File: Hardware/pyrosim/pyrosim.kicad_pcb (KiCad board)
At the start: 2 copper layers, 13 x 15.5 mm, 7 parts, among them J1 Conn_01x04_Pin

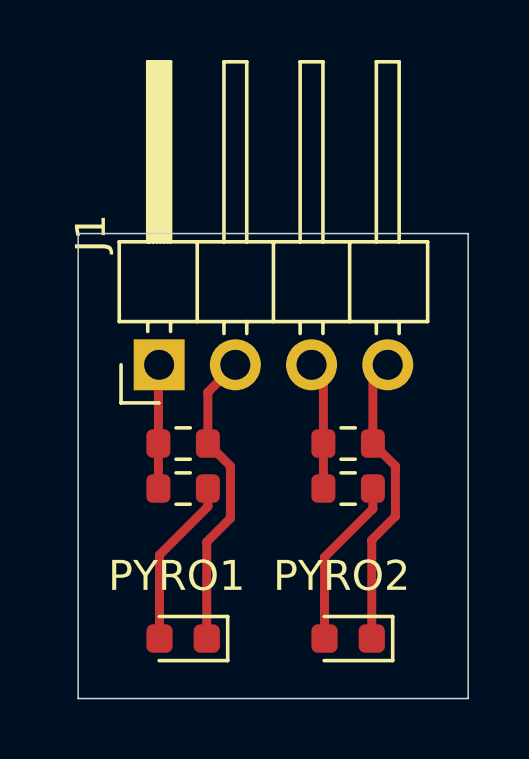
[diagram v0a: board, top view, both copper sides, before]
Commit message: APRS emulation testing, trying to get long packets working
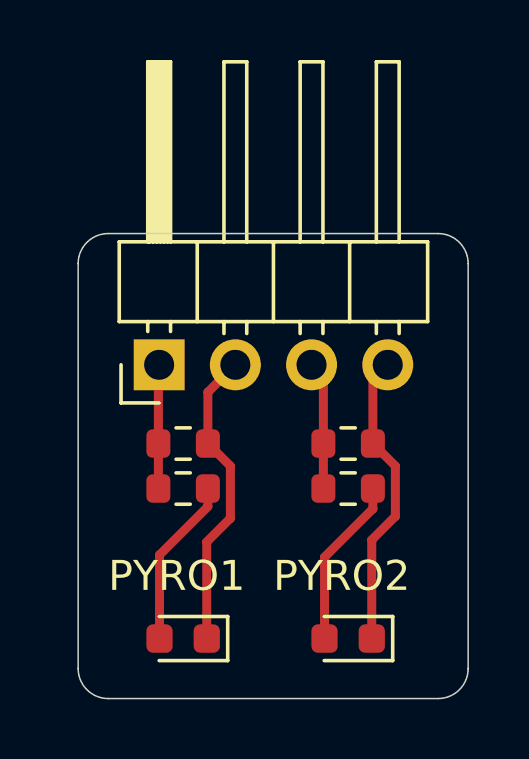
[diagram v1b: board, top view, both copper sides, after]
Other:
- outline, holes or cut-outs redrawn
- board text added: "PYROSIM"
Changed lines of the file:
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@@
 		)
 		(property "Value" "470R"
-			(at 0 1.43 360)
+			(at 0 1.43 0)
 			(layer "F.Fab")
 			(effects
@@
 		)
 		(fp_text user "${REFERENCE}"
-			(at 0 0 360)
+			(at 0 0 0)
 			(layer "F.Fab")
 			(effects
@@
 			(at 4.385 -2.27 90)
 			(layer "F.SilkS")
+			(hide yes)
 			(effects
 				(font
@@
 		)
 		(fp_text user "${REFERENCE}"
-			(at 2.77 3.81 360)
+			(at 2.77 3.81 0)
 			(layer "F.Fab")
 			(effects
@@
 		)
 		(property "Value" "470R"
-			(at 0 1.43 360)
+			(at 0 1.43 0)
 			(layer "F.Fab")
 			(effects
@@
 		)
 		(fp_text user "${REFERENCE}"
-			(at 0 0 360)
+			(at 0 0 0)
 			(layer "F.Fab")
 			(effects
@@
 		)
 		(property "Value" "LED"
-			(at 0 1.43 360)
+			(at 0 1.43 0)
 			(layer "F.Fab")
 			(effects
@@
 		)
 		(fp_text user "${REFERENCE}"
-			(at 0 0 360)
+			(at 0 0 0)
 			(layer "F.Fab")
 			(effects
@@
 		)
 		(property "Value" "470R"
-			(at 0 1.43 360)
+			(at 0 1.43 0)
 			(layer "F.Fab")
 			(effects
@@
 		)
 		(fp_text user "${REFERENCE}"
-			(at 0 0 360)
+			(at 0 0 0)
 			(layer "F.Fab")
 			(effects
@@
 		)
 		(property "Value" "LED"
-			(at 0 1.43 360)
+			(at 0 1.43 0)
 			(layer "F.Fab")
 			(effects
@@
 		)
 		(fp_text user "${REFERENCE}"
-			(at 0 0 360)
+			(at 0 0 0)
 			(layer "F.Fab")
 			(effects
@@
 		)
 	)
-	(gr_rect
-		(start 122 79)
-		(end 135 94.5)
+	(gr_arc
+		(start 135 93.5)
+		(mid 134.707107 94.207107)
+		(end 134 94.5)
 		(stroke
 			(width 0.05)
 			(type default)
 		)
-		(fill none)
 		(layer "Edge.Cuts")
 	)
+	(gr_line
+		(start 122 93.5)
+		(end 122 80)
+		(stroke
+			(width 0.05)
+			(type default)
+		)
+		(layer "Edge.Cuts")
+	)
+	(gr_arc
+		(start 123 94.5)
+		(mid 122.292893 94.207107)
+		(end 122 93.5)
+		(stroke
+			(width 0.05)
+			(type default)
+		)
+		(layer "Edge.Cuts")
+	)
+	(gr_line
+		(start 123 79)
+		(end 134 79)
+		(stroke
+			(width 0.05)
+			(type default)
+		)
+		(layer "Edge.Cuts")
+	)
+	(gr_arc
+		(start 134 79)
+		(mid 134.707107 79.292893)
+		(end 135 80)
+		(stroke
+			(width 0.05)
+			(type default)
+		)
+		(layer "Edge.Cuts")
+	)
+	(gr_line
+		(start 134 94.5)
+		(end 123 94.5)
+		(stroke
+			(width 0.05)
+			(type default)
+		)
+		(layer "Edge.Cuts")
+	)
+	(gr_line
+		(start 135 80)
+		(end 135 93.5)
+		(stroke
+			(width 0.05)
+			(type default)
+		)
+		(layer "Edge.Cuts")
+	)
+	(gr_arc
+		(start 122 80)
+		(mid 122.292893 79.292893)
+		(end 123 79)
+		(stroke
+			(width 0.05)
+			(type default)
+		)
+		(layer "Edge.Cuts")
+	)
+	(gr_text "PYROSIM"
+		(at 131.7 94 -0)
+		(layer "B.SilkS")
+		(effects
+			(font
+				(size 1 1)
+				(thickness 0.15)
+			)
+			(justify left bottom mirror)
+		)
+	)
 	(gr_text "PYRO2"
